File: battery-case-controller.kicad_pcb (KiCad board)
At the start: 6 copper layers, 110 x 55 mm, 168 parts, among them J21 Display, J22 HALL, J23 MOT_AUX, J24 CRANK, J25 CAN_IN, J26 CAN_OUT, J27 +, J28 A, J29 B, J30 C, J31 GND, M21 MountingHole_Pad, M22 MountingHole_Pad, M23 MountingHole_Pad, Q21 BSC040N08, Q22 BSC040N08, Q23 BSC040N08, Q24 BSC040N08, Q25 BSC040N08, Q26 BSC040N08, U21 Enable, U22 LM5109B, U23 INA240A2PWR, U24 LM5109B, U25 INA240A2PWR, U26 LM5109B, U27 INA240A2PWR, U28 LMR12010X, U29 LM5008, U30 XC6206P332MR, U31 XC6206P332MR, U32 SN65HVD230, U33 15p, U34 100n, U35 8MHz, U36 10u, U37 15p, U38 10u, U39 100n, U40 100n, U41 100n, U42 100n, U43 100n, U44 STM32G491CxT, U45 SWD, U46 RUN, U47 470R, U48 ERROR, U49 470R, U50 PWM, U51 470R, U52 1u, U53 100n, U54 Debug

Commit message: Placing first round finished
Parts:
- removed the C51 at (234.8, 106.4)
- removed the U42 at (337.9, 82.8)
- removed U43: 100n, Capacitor_SMD:C_0603_1608Metric
- added C65: 10u, Capacitor_SMD:C_2220_5650Metric, F.Cu at (114.2, 98.0)
- added Q32: BSC040N08, Package_TO_SOT_SMD:TDSON-8-1, F.Cu at (151.0, 124.3)
- added Q34: BSC040N08, Package_TO_SOT_SMD:TDSON-8-1, F.Cu at (164.2, 124.3)
- added Q36: BSC040N08, Package_TO_SOT_SMD:TDSON-8-1, F.Cu at (138.0, 124.3)
- added Q38: BSC040N08, Package_TO_SOT_SMD:TDSON-8-1, F.Cu at (125.0, 124.3)
- added Q40: BSC040N08, Package_TO_SOT_SMD:TDSON-8-1, F.Cu at (183.8, 124.3)
- added Q42: BSC040N08, Package_TO_SOT_SMD:TDSON-8-1, F.Cu at (196.8, 124.3)
- added R36: 22R, Resistor_SMD:R_0603_1608Metric, F.Cu at (149.0, 119.0)
- added R39: 22R, Resistor_SMD:R_0603_1608Metric, F.Cu at (160.5, 119.0)
- added R43: 22R, Resistor_SMD:R_0603_1608Metric, F.Cu at (136.0, 119.0)
- added R46: 22R, Resistor_SMD:R_0603_1608Metric, F.Cu at (121.8, 119.0)
- added R50: 22R, Resistor_SMD:R_0603_1608Metric, F.Cu at (181.8, 119.1)
- added R53: 22R, Resistor_SMD:R_0603_1608Metric, F.Cu at (195.2, 119.0)
- J21: renamed from U54; footprint Connector_USB:USB_Micro-B_Wuerth_614105150721_Vertical -> Connector_USB:USB_Micro-AB_Molex_47590-0001
- moved C23 181.2 mm to (164.7, 84.1)
- moved R21 177.5 mm to (164.5, 77.0), turned to -90 degrees
- moved C24 177.2 mm to (164.7, 82.6)
- moved R22 172.8 mm to (168.0, 77.0), turned to 90 degrees
- moved C28 170.5 mm to (168.2, 81.4)
- moved X21 169.8 mm to (162.9, 86.9)
- moved C75 169.0 mm to (136.0, 100.0), turned to 180 degrees
- moved C29 166.7 mm to (180.2, 85.6)
- moved C21 166.4 mm to (171.9, 97.9), turned to -90 degrees
- moved C27 166.3 mm to (177.2, 98.1), turned to -90 degrees
- moved R59 166.3 mm to (103.2, 100.7), turned to 180 degrees
- moved D21 166.0 mm to (166.2, 77.0), turned to -90 degrees
- moved R23 165.3 mm to (171.5, 77.0), turned to -90 degrees
- moved C26 163.9 mm to (175.2, 98.1), turned to -90 degrees
- moved R74 163.3 mm to (134.2, 82.0), turned to 180 degrees
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- renumbered U52 to C21, U53 to C22, U33 to C23, U37 to C24, U34 to C25, U36 to C26, U38 to C27, U39 to C28, U40 to C29, U41 to C30, C21 to C31, C22 to C32, C28 to C33, C29 to C34, C30 to C35, C25 to C36, C26 to C37, C23 to C38, C24 to C39, C31 to C40, C27 to C41, C37 to C42, C38 to C43, C39 to C44, C34 to C45, C35 to C46, C32 to C47, C33 to C48, C40 to C49, C36 to C50, C46 to C51, C47 to C52, C48 to C53, C43 to C54, C44 to C55, C41 to C56, C42 to C57, C49 to C58, C45 to C59, C56 to C60, C59 to C61, C53 to C62, C61 to C63, C62 to C64, C52 to C66, C63 to C67, C64 to C68, C54 to C69, C55 to C70, C57 to C71, C58 to C72, C60 to C73, C50 to C74, C72 to C75, C65 to C76, C66 to C77, C67 to C78, C69 to C79, C70 to C80, C68 to C81, C71 to C82, U46 to D21, U48 to D22, U50 to D23, D21 to D31, D22 to D32, D23 to D33, D26 to D34, D27 to D35, D29 to D36, D25 to D37, D24 to D38, D28 to D39, D30 to D40, FB21 to FB31, FB22 to FB32, FB23 to FB33, U45 to J22, J27 to J31, J21 to J32, J28 to J33, J22 to J34, J29 to J35, J23 to J36, J30 to J37, J24 to J38, J31 to J39, J25 to J40, J26 to J41, L22 to L31, L21 to L32, M21 to M31, M22 to M32, M23 to M33, Q21 to Q31, Q22 to Q33, Q23 to Q35, Q24 to Q37, Q25 to Q39, Q26 to Q41, U47 to R21, U49 to R22, U51 to R23, R21 to R31, R23 to R32, R24 to R33, R22 to R34, R25 to R35, R29 to R37, R26 to R38, R27 to R40, R28 to R41, R30 to R42, R34 to R44, R31 to R45, R32 to R47, R33 to R48, R35 to R49, R39 to R51, R36 to R52, R37 to R54, R38 to R55, R40 to R56, R47 to R57, R48 to R58, R44 to R59, R41 to R60, R45 to R61, R43 to R62, R46 to R63, R42 to R64, R49 to R65, R50 to R66, R51 to R67, R52 to R68, R61 to R69, R53 to R70, R54 to R71, R55 to R72, R56 to R73, R67 to R74, R57 to R75, R64 to R76, R58 to R77, R65 to R78, R66 to R79, R62 to R80, R59 to R81, R60 to R82, R63 to R83, U44 to U21, U21 to U31, U22 to U32, U23 to U33, U24 to U34, U25 to U35, U26 to U36, U27 to U37, U29 to U38, U31 to U39, U30 to U40, U28 to U41, U32 to U42, U35 to X21
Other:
- outline, holes or cut-outs redrawn

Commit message: layout
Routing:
- net Net-(Q35-Pad4): track 0.00 -> 1.77 mm
- net Net-(C45-Pad2): vias 0 -> 57
- net GNDPWR: vias 0 -> 68
- net +BATT: vias 0 -> 66
- added copper zone on In2.Cu, net +3V3
- added copper zone on F.Cu, net +BATT
- added copper zone on In2.Cu, net +BATT
- added copper zone on In4.Cu, net +BATT
- added copper zone on B.Cu, net /phase_a/Phase
- added copper zone on F.Cu, net /phase_a/Phase
- added copper zone on B.Cu, net /phase_b/Phase
- added copper zone on F.Cu, net /phase_b/Phase
- added copper zone on B.Cu, net /phase_c/Phase
- added copper zone on F.Cu, net /phase_c/Phase
- added copper zone on In3.Cu, net GNDD
- added copper zone on F.Cu, net GNDPWR
- added copper zone on In3.Cu, net GNDPWR
- added copper zone on B.Cu, net Net-(C45-Pad2)
- added copper zone on F.Cu, net Net-(C45-Pad2)

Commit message: next round routing
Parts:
- moved FB31 17.8 mm to (119.8, 102.8), turned to -90 degrees
- moved R56 6.85 mm to (109.5, 97.8), turned to 90 degrees
- moved C75 5.99 mm to (138.8, 94.7)
- moved U42 5.99 mm to (138.8, 89.7)
- moved C62 3.97 mm to (106.2, 104.0), turned to 0 degrees
- moved D32 3.81 mm to (124.0, 105.5)
- moved C60 2.98 mm to (106.6, 95.8), turned to 180 degrees
- moved R60 2.85 mm to (103.4, 95.8)
- moved D37 2.53 mm to (126.8, 85.3)
- moved R64 1.39 mm to (120.1, 89.7), turned to 0 degrees
- moved C69 1.23 mm to (131.1, 93.8)
- moved C70 1.23 mm to (131.1, 96.0)
- moved C71 1.23 mm to (131.0, 98.3)
- moved D38 1.23 mm to (127.0, 96.3)
- moved R62 1.17 mm to (120.1, 91.5), turned to 180 degrees
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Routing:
- net +12V: track 0.00 -> 83.6 mm, vias 0 -> 10
- net GNDPWR: track 0.00 -> 80.7 mm, vias 68 -> 55
- net Net-(C54-Pad2): track 0.00 -> 35.7 mm, vias 0 -> 60
- net Net-(R49-Pad2): track 0.00 -> 33.9 mm, vias 0 -> 2
- net /power_supply/DCDC_VIN: track 0.00 -> 30.6 mm
- net Net-(R38-Pad2): track 0.00 -> 26.3 mm, vias 0 -> 3
- net Net-(R45-Pad2): track 0.00 -> 25.8 mm, vias 0 -> 3
- net Net-(R52-Pad2): track 0.00 -> 23.5 mm
- net Net-(C45-Pad2): track 0.00 -> 22.4 mm, vias 57 -> 59
- net Net-(R42-Pad2): track 0.00 -> 21.5 mm, vias 0 -> 2
- net Net-(C61-Pad1): track 0.00 -> 19.6 mm
- net Net-(C36-Pad2): track 0.00 -> 13.7 mm, vias 0 -> 86
- net Net-(R35-Pad2): track 0.00 -> 12.8 mm, vias 0 -> 2
- net Net-(C54-Pad1): track 0.00 -> 9.58 mm
- net Net-(C45-Pad1): track 0.00 -> 7.81 mm
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- added copper zone on F.Cu, net +12V
- added copper zone on In1.Cu, net +12V
- added copper zone on B.Cu, net +BATT
- added copper zone on F.Cu, net /power_supply/DCDC_VIN
- added copper zone on F.Cu, net GNDD
- added copper zone on B.Cu, net GNDPWR
- added copper zone on B.Cu, net Net-(C36-Pad2)
- added copper zone on F.Cu, net Net-(C36-Pad2)
- added copper zone on B.Cu, net Net-(C54-Pad2)
- added copper zone on F.Cu, net Net-(C54-Pad2)
- added copper zone on F.Cu, net Net-(C60-Pad1)
- added copper zone on F.Cu, net Net-(C61-Pad1)
- added copper zone on F.Cu, net Net-(C66-Pad1)

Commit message: just the silk open
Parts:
- added C41: 100n, Capacitor_SMD:C_0603_1608Metric, F.Cu at (154.8, 100.8)
- added C42: 2n2, Capacitor_SMD:C_0603_1608Metric, F.Cu at (161.4, 91.8)
- added C52: 100n, Capacitor_SMD:C_0603_1608Metric, F.Cu at (154.7, 95.5)
- added C53: 2n2, Capacitor_SMD:C_0603_1608Metric, F.Cu at (161.4, 90.1)
- added C63: 100n, Capacitor_SMD:C_0603_1608Metric, F.Cu at (185.0, 99.5)
- added C64: 2n2, Capacitor_SMD:C_0603_1608Metric, F.Cu at (168.8, 97.9)
- added R41: 1k, Resistor_SMD:R_0603_1608Metric, F.Cu at (158.0, 95.5)
- added R49: 1k, Resistor_SMD:R_0603_1608Metric, F.Cu at (158.1, 90.0)
- added R57: 1k, Resistor_SMD:R_0603_1608Metric, F.Cu at (181.6, 99.5)
- moved C78 16.0 mm to (134.2, 98.2), turned to 90 degrees
- moved U40 12.2 mm to (136.9, 98.2), turned to 90 degrees
- moved C79 12.0 mm to (136.9, 101.2), turned to 0 degrees
- moved R34 8.70 mm to (156.4, 118.0)
- moved FB32 8.03 mm to (139.9, 98.5), turned to 90 degrees
- moved C51 7.10 mm to (157.4, 92.7)
- moved C40 6.80 mm to (157.2, 98.2)
- moved FB33 6.10 mm to (141.2, 101.2), turned to 180 degrees
- moved C31 5.86 mm to (182.2, 82.1)
- moved C73 5.71 mm to (141.7, 98.5), turned to 90 degrees
- moved R77 5.60 mm to (135.2, 87.5), turned to 90 degrees
- moved U35 4.67 mm to (152.5, 92.7)
- moved R58 4.49 mm to (182.2, 88.8)
- moved U33 4.35 mm to (152.4, 98.2)
- moved C82 4.13 mm to (182.2, 85.5)
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- renumbered C41 to C43, C42 to C44, C43 to C45, C44 to C46, C45 to C47, C46 to C48, C47 to C49, C48 to C50, C49 to C51, C50 to C54, C51 to C55, C52 to C56, C53 to C57, C54 to C58, C55 to C59, C56 to C60, C57 to C61, C58 to C62, C59 to C65, C60 to C66, C61 to C67, C62 to C68, C63 to C69, C64 to C70, C65 to C71, C66 to C72, C67 to C73, C68 to C74, C69 to C75, C70 to C76, C71 to C77, C72 to C78, C73 to C79, C74 to C80, C75 to C81, C76 to C82, C77 to C83, C78 to C84, C79 to C85, C80 to C86, C81 to C87, C82 to C88, C21 to C89, C22 to C90, C23 to C91, C24 to C92, C25 to C93, C26 to C94, C27 to C95, C28 to C96, C29 to C97, C30 to C98, D21 to D41, D22 to D42, D23 to D43, J21 to J42, J22 to J43, R41 to R42, R42 to R43, R43 to R44, R44 to R45, R45 to R46, R46 to R47, R47 to R48, R48 to R50, R49 to R51, R50 to R52, R51 to R53, R52 to R54, R53 to R55, R54 to R56, R55 to R58, R56 to R59, R57 to R60, R58 to R61, R59 to R62, R60 to R63, R61 to R64, R62 to R65, R63 to R66, R64 to R67, R65 to R68, R66 to R69, R67 to R70, R68 to R71, R69 to R72, R70 to R73, R71 to R74, R72 to R75, R73 to R76, R74 to R77, R75 to R78, R76 to R79, R77 to R80, R78 to R81, R79 to R82, R80 to R83, R81 to R84, R82 to R85, R83 to R86, R21 to R87, R22 to R88, R23 to R89, U21 to U43, X21 to X31
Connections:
- U33 pad 8: /mcu/AIN_IB -> Net-(U33-Pad8)
- U35 pad 8: /mcu/AIN_IA -> Net-(U35-Pad8)
- U37 pad 8: /mcu/AIN_IC -> Net-(U37-Pad8)
- U43 pad 25: unconnected-(U21-Pad25) -> /Interface/PWM_BREAK
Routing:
- net GNDA: track 0.00 -> 101.3 mm, vias 0 -> 14
- net /Interface/VREF: track 0.00 -> 86.0 mm, vias 0 -> 5
- net /mcu/AIN_TEMP: track 0.00 -> 79.2 mm, vias 0 -> 2
- net /mcu/DISP_RX: track 0.00 -> 74.1 mm, vias 0 -> 1
- net +5V: track 5.67 -> 78.9 mm, vias 0 -> 1
- net /mcu/PWM_A: track 0.00 -> 72.9 mm, vias 0 -> 2
- net /mcu/DISP_TX: track 0.00 -> 69.0 mm, vias 0 -> 1
- net /mcu/PWM_AN: track 0.00 -> 67.4 mm, vias 0 -> 2
- net /Interface/PULSE_CRK: track 0.00 -> 61.3 mm, vias 0 -> 2
- net /mcu/PWM_B: track 0.00 -> 59.4 mm, vias 0 -> 2
- net /mcu/PWM_BN: track 0.00 -> 52.8 mm, vias 0 -> 2
- net /mcu/AIN_VB: track 0.00 -> 52.2 mm, vias 0 -> 2
- net /mcu/PWM_C: track 0.00 -> 50.9 mm, vias 0 -> 2
- net /mcu/AIN_VC: track 0.00 -> 50.6 mm, vias 0 -> 2
- net /mcu/PWM_CN: track 0.00 -> 50.5 mm, vias 0 -> 2
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- added copper zone on B.Cu, net +3.3VADC
- added copper zone on F.Cu, net +5V
- added copper zone on F.Cu, net GNDA
- added copper zone on In1.Cu, net GNDA

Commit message: Ordered
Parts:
- D42: value ERROR -> ERR
- J32: value Display -> DISPLAY
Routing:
- net GNDA: track 101.3 -> 96.7 mm
- net +12V: track 131.8 -> 128.5 mm
- net Net-(R65-Pad1): track 7.53 -> 7.01 mm
- net Net-(C36-Pad2): vias 87 -> 86

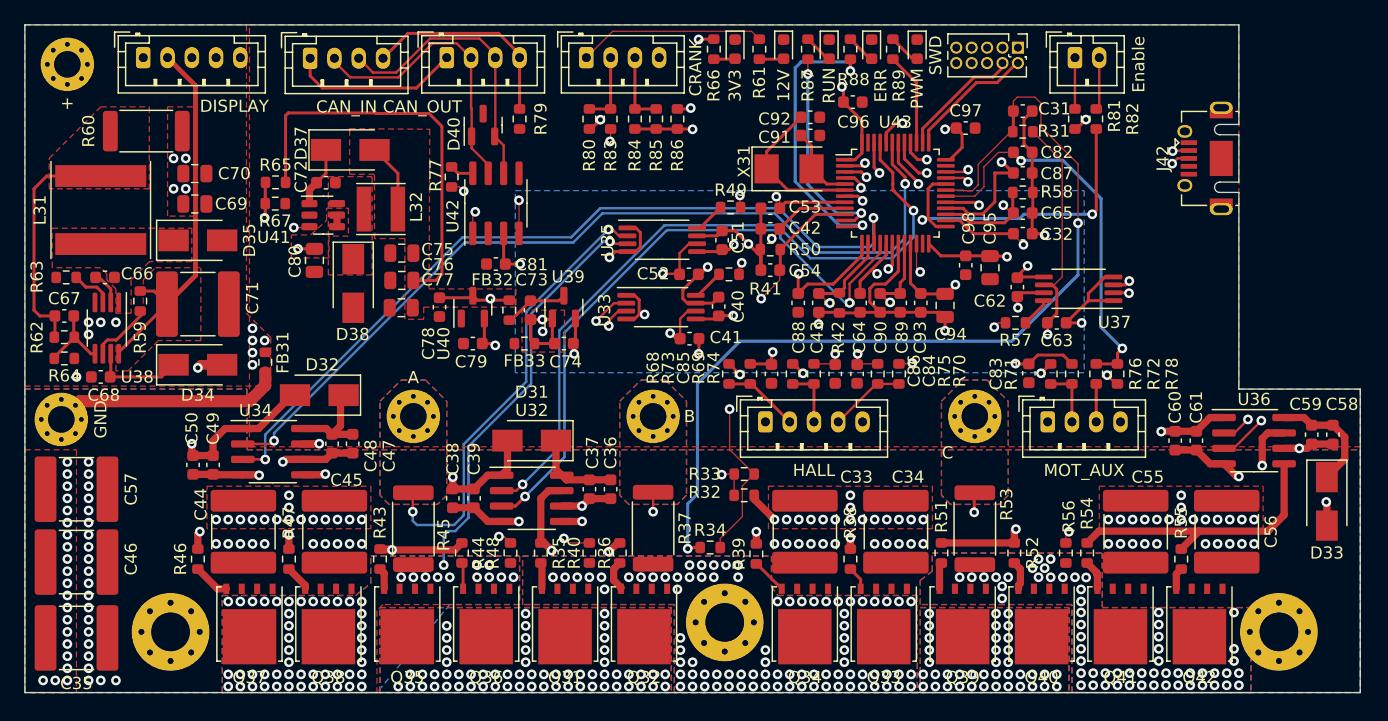
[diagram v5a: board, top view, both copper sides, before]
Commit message: Fixed SWD connector spacing and fit of pcb to housing
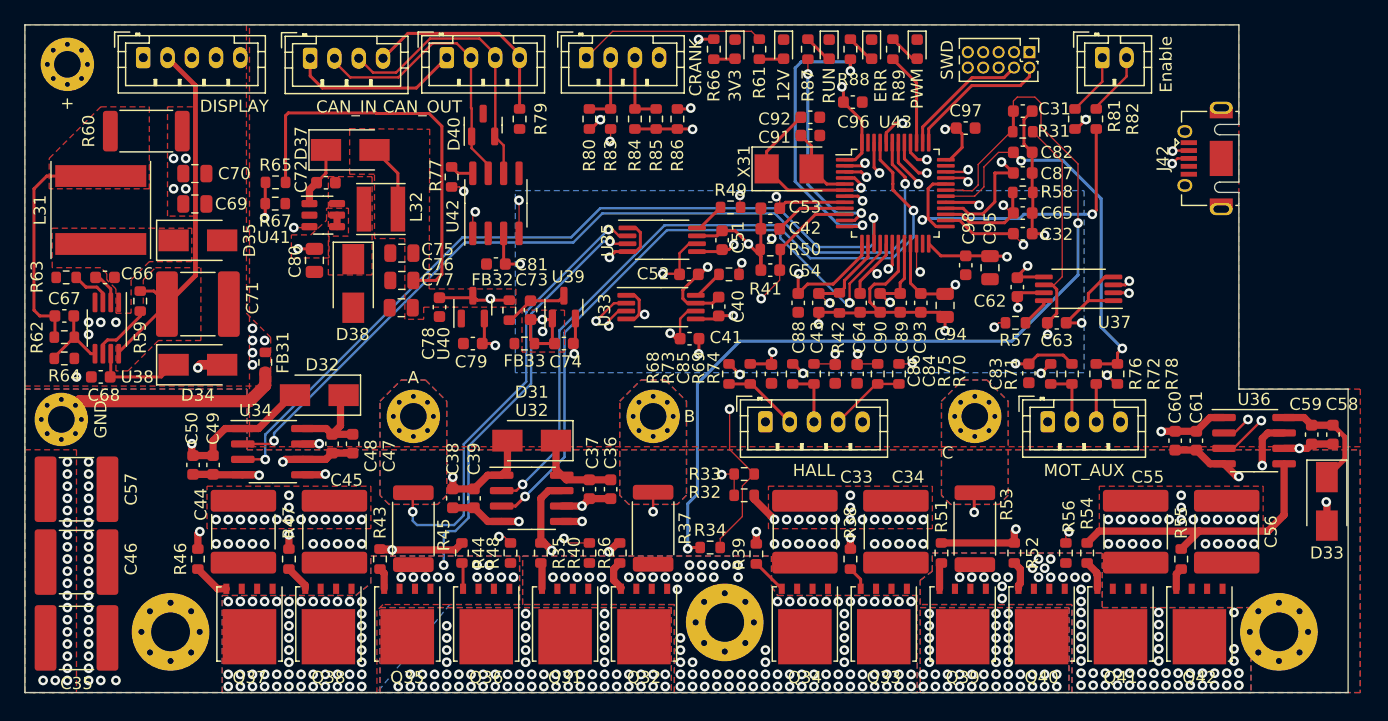
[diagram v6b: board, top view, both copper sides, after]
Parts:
- moved U31 2.25 mm to (188.8, 77.7)
- moved J43 1.02 mm to (182.8, 77.2)
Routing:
- net /mcu/SWD_IO: track 10.7 -> 12.0 mm
- net /Interface/ENABLE+: track 4.22 -> 5.16 mm
- net /Interface/ENABLE-: track 4.33 -> 5.26 mm
- net /mcu/SWD_CLK: track 10.2 -> 10.8 mm
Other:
- board size 110 x 55 mm -> 109 x 55 mm
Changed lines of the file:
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@@
   )
   (footprint "Connector_JST:JST_PH_B2B-PH-K_1x02_P2.00mm_Vertical" (layer "F.Cu")
-    (at 186.5 77.7)
+    (at 188.75 77.7)
     (descr "JST PH series connector, B2B-PH-K (http://www.jst-mfg.com/product/pdf/eng/ePH.pdf), generated with kicad-footprint-generator")
     (tags "connector JST PH side entry")
@@
   )
   (footprint "Connector_PinHeader_1.27mm:PinHeader_2x05_P1.27mm_Vertical" (layer "F.Cu")
-    (at 181.8 76.875 -90)
+    (at 182.75 77.25 -90)
     (descr "Through hole straight pin header, 2x05, 1.27mm pitch, double rows")
     (tags "Through hole pin header THT 2x05 1.27mm double row")
@@
   (gr_line locked (start 210 125) (end 100 125) (layer "Dwgs.User") (width 0.15))
   (gr_line locked (start 100 110) (end 210 110) (layer "Dwgs.User") (width 0.15))
-  (gr_line (start 100 130) (end 210 130) (layer "Edge.Cuts") (width 0.1))
+  (gr_line (start 100 130) (end 209 130) (layer "Edge.Cuts") (width 0.1))
   (gr_line locked (start 100 75) (end 100 130) (layer "Edge.Cuts") (width 0.1))
   (gr_line (start 200 82.25) (end 200 75) (layer "Edge.Cuts") (width 0.1))
   (gr_line locked (start 200 75) (end 100 75) (layer "Edge.Cuts") (width 0.1))
-  (gr_line locked (start 210 130) (end 210 105) (layer "Edge.Cuts") (width 0.1))
-  (gr_line locked (start 200 105) (end 210 105) (layer "Edge.Cuts") (width 0.1))
+  (gr_line locked (start 209 130) (end 209 105) (layer "Edge.Cuts") (width 0.1))
+  (gr_line locked (start 200 105) (end 209 105) (layer "Edge.Cuts") (width 0.1))
   (gr_line (start 200 105) (end 200 89.75) (layer "Edge.Cuts") (width 0.1))
   (dimension (type aligned) (layer "Dwgs.User")
@@
   (segment (start 148.5 119.825) (end 149 119.325) (width 0.6) (layer "F.Cu") (net 40))
   (segment (start 149.095 121.345) (end 148.5 120.75) (width 0.6) (layer "F.Cu") (net 40))
-  (segment (start 186.5 77.7) (end 186.5 81.925) (width 0.2) (layer "F.Cu") (net 41))
-  (segment (start 188.5 81.675) (end 188.25 81.925) (width 0.2) (layer "F.Cu") (net 42))
-  (segment (start 188.5 77.7) (end 188.5 81.675) (width 0.2) (layer "F.Cu") (net 42))
+  (segment (start 186.5 81.925) (end 188.75 79.675) (width 0.2) (layer "F.Cu") (net 41))
+  (segment (start 188.75 79.675) (end 188.75 77.7) (width 0.2) (layer "F.Cu") (net 41))
+  (segment (start 190.75 79.25) (end 190.75 77.7) (width 0.2) (layer "F.Cu") (net 42))
+  (segment (start 188.25 81.925) (end 188.25 81.75) (width 0.2) (layer "F.Cu") (net 42))
+  (segment (start 188.25 81.75) (end 190.75 79.25) (width 0.2) (layer "F.Cu") (net 42))
   (segment (start 174.4 88.5) (end 174.79 88.11) (width 0.25) (layer "F.Cu") (net 43))
   (segment (start 174.4 90.950685) (end 174.039479 90.950685) (width 0.25) (layer "F.Cu") (net 43))
@@
   (via (at 169.004279 89.495721) (size 0.8) (drill 0.4) (layers "F.Cu" "B.Cu") (net 56))
   (segment (start 174.568589 89.495721) (end 169.004279 89.495721) (width 0.25) (layer "In1.Cu") (net 56))
-  (segment (start 176.72 78.145) (end 176.72 87.34431) (width 0.25) (layer "In1.Cu") (net 56))
+  (segment (start 176.72 87.34431) (end 176.72 79.47) (width 0.25) (layer "In1.Cu") (net 56))
+  (segment (start 176.72 79.47) (end 177.67 78.52) (width 0.25) (layer "In1.Cu") (net 56))
   (segment (start 176.72 87.34431) (end 174.568589 89.495721) (width 0.25) (layer "In1.Cu") (net 56))
   (segment (start 177.370901 87.61) (end 177.688399 87.927498) (width 0.2) (layer "F.Cu") (net 57))
@@
   (segment (start 195.3995 84.960257) (end 194.989743 84.5505) (width 0.2) (layer "In4.Cu") (net 58))
   (segment (start 191.9505 86.9995) (end 177.770947 86.9995) (width 0.2) (layer "In4.Cu") (net 58))
-  (segment (start 181.8 78.145) (end 181.696727 78.145) (width 0.25) (layer "F.Cu") (net 59))
-  (segment (start 181.696727 78.145) (end 180.091727 79.75) (width 0.25) (layer "F.Cu") (net 59))
-  (segment (start 174.45 83.686396) (end 174.45 84.6975) (width 0.25) (layer "F.Cu") (net 59))
-  (segment (start 178.386396 79.75) (end 174.45 83.686396) (width 0.25) (layer "F.Cu") (net 59))
-  (segment (start 180.091727 79.75) (end 178.386396 79.75) (width 0.25) (layer "F.Cu") (net 59))
-  (segment (start 173.95 83.55) (end 173.95 84.6975) (width 0.25) (layer "F.Cu") (net 60))
-  (segment (start 180.555 78.495) (end 179.75 79.3) (width 0.25) (layer "F.Cu") (net 60))
-  (segment (start 178.2 79.3) (end 173.95 83.55) (width 0.25) (layer "F.Cu") (net 60))
-  (segment (start 180.555 78.145) (end 180.555 78.495) (width 0.25) (layer "F.Cu") (net 60))
-  (segment (start 179.75 79.3) (end 178.2 79.3) (width 0.25) (layer "F.Cu") (net 60))
+  (segment (start 178 80) (end 182 80) (width 0.25) (layer "F.Cu") (net 59))
+  (segment (start 174.45 83.55) (end 178 80) (width 0.25) (layer "F.Cu") (net 59))
+  (segment (start 182 80) (end 182.75 79.25) (width 0.25) (layer "F.Cu") (net 59))
+  (segment (start 174.45 84.6975) (end 174.45 83.55) (width 0.25) (layer "F.Cu") (net 59))
+  (segment (start 182.75 79.25) (end 182.75 78.52) (width 0.25) (layer "F.Cu") (net 59))
+  (segment (start 180.655 79.345) (end 181.48 78.52) (width 0.25) (layer "F.Cu") (net 60))
+  (segment (start 173.95 83.41431) (end 178.01931 79.345) (width 0.25) (layer "F.Cu") (net 60))
+  (segment (start 178.01931 79.345) (end 180.655 79.345) (width 0.25) (layer "F.Cu") (net 60))
+  (segment (start 173.95 84.6975) (end 173.95 83.41431) (width 0.25) (layer "F.Cu") (net 60))
   (segment (start 148.25 112.475) (end 146.5 112.475) (width 0.6) (layer "F.Cu") (net 61))
   (segment (start 143.75 109.25) (end 143.75 111.62) (width 0.6) (layer "F.Cu") (net 61))
@@
   (segment (start 136.55 115.6) (end 135.45 116.7) (width 0.2) (layer "B.Cu") (net 81))
   (segment (start 136.55 109.7) (end 136.55 115.6) (width 0.2) (layer "B.Cu") (net 81))
-  (segment (start 208.725 108.95) (end 208.725 110.775) (width 0.6) (layer "F.Cu") (net 82))
+  (segment (start 208.725 108.95) (end 208.725 110.775) (width 0.4) (layer "F.Cu") (net 82))
   (segment (start 205.37 107.345) (end 206 107.975) (width 0.6) (layer "F.Cu") (net 82))
-  (segment (start 208.725 110.775) (end 207.25 112.25) (width 0.6) (layer "F.Cu") (net 82))
-  (segment (start 207.75 107.975) (end 208.725 108.95) (width 0.6) (layer "F.Cu") (net 82))
+  (segment (start 208.725 110.775) (end 207.25 112.25) (width 0.4) (layer "F.Cu") (net 82))
+  (segment (start 207.75 107.975) (end 208.725 108.95) (width 0.4) (layer "F.Cu") (net 82))
   (segment (start 206 107.975) (end 207.75 107.975) (width 0.6) (layer "F.Cu") (net 82))
   (segment (start 203.725 107.345) (end 205.37 107.345) (width 0.6) (layer "F.Cu") (net 82))
